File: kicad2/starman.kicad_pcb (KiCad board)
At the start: 4 copper layers, 195 x 150 mm, 202 parts, among them J1 Conn_01x12, J10 Barrel_Jack_MountingPin, J2 Conn_01x10, J3 Conn_01x12, J4 Conn_01x06, J5 Conn_02x03_Counter_Clockwise, J6 Conn_01x12, J7 Conn_01x10, J8 Conn_01x12, J9 Conn_01x08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

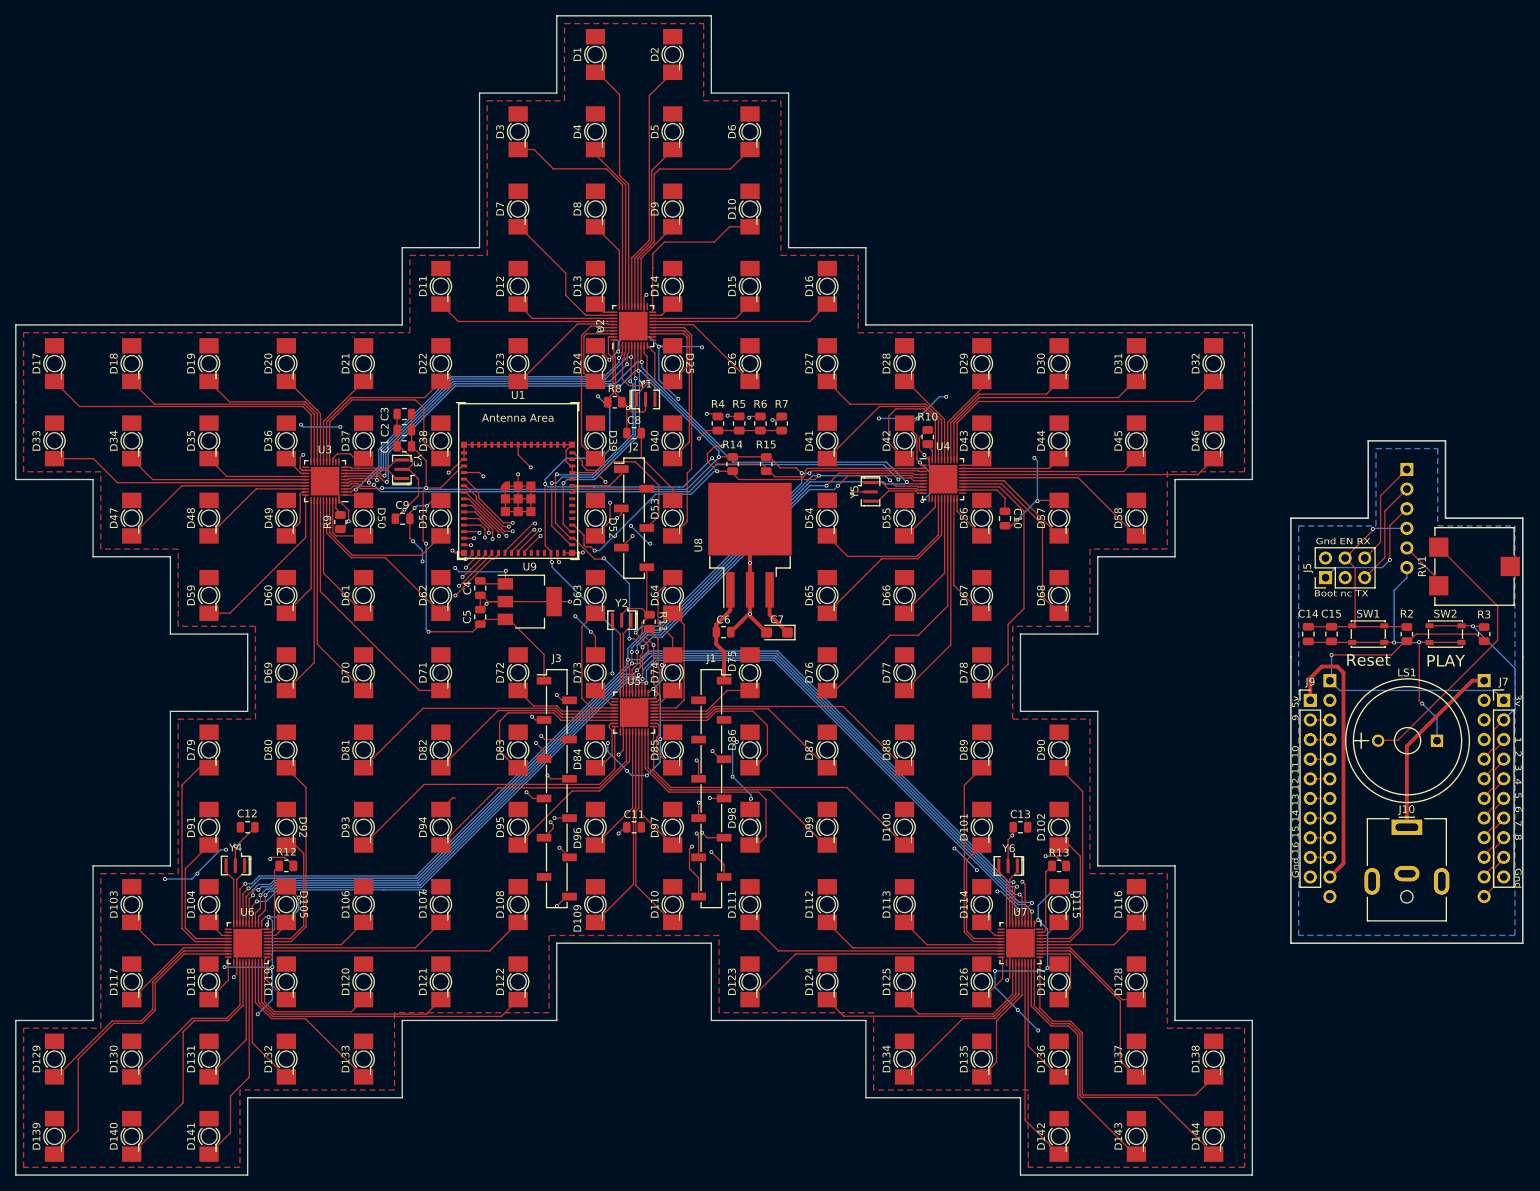
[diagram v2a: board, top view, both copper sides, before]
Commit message: Added dimensions and a label
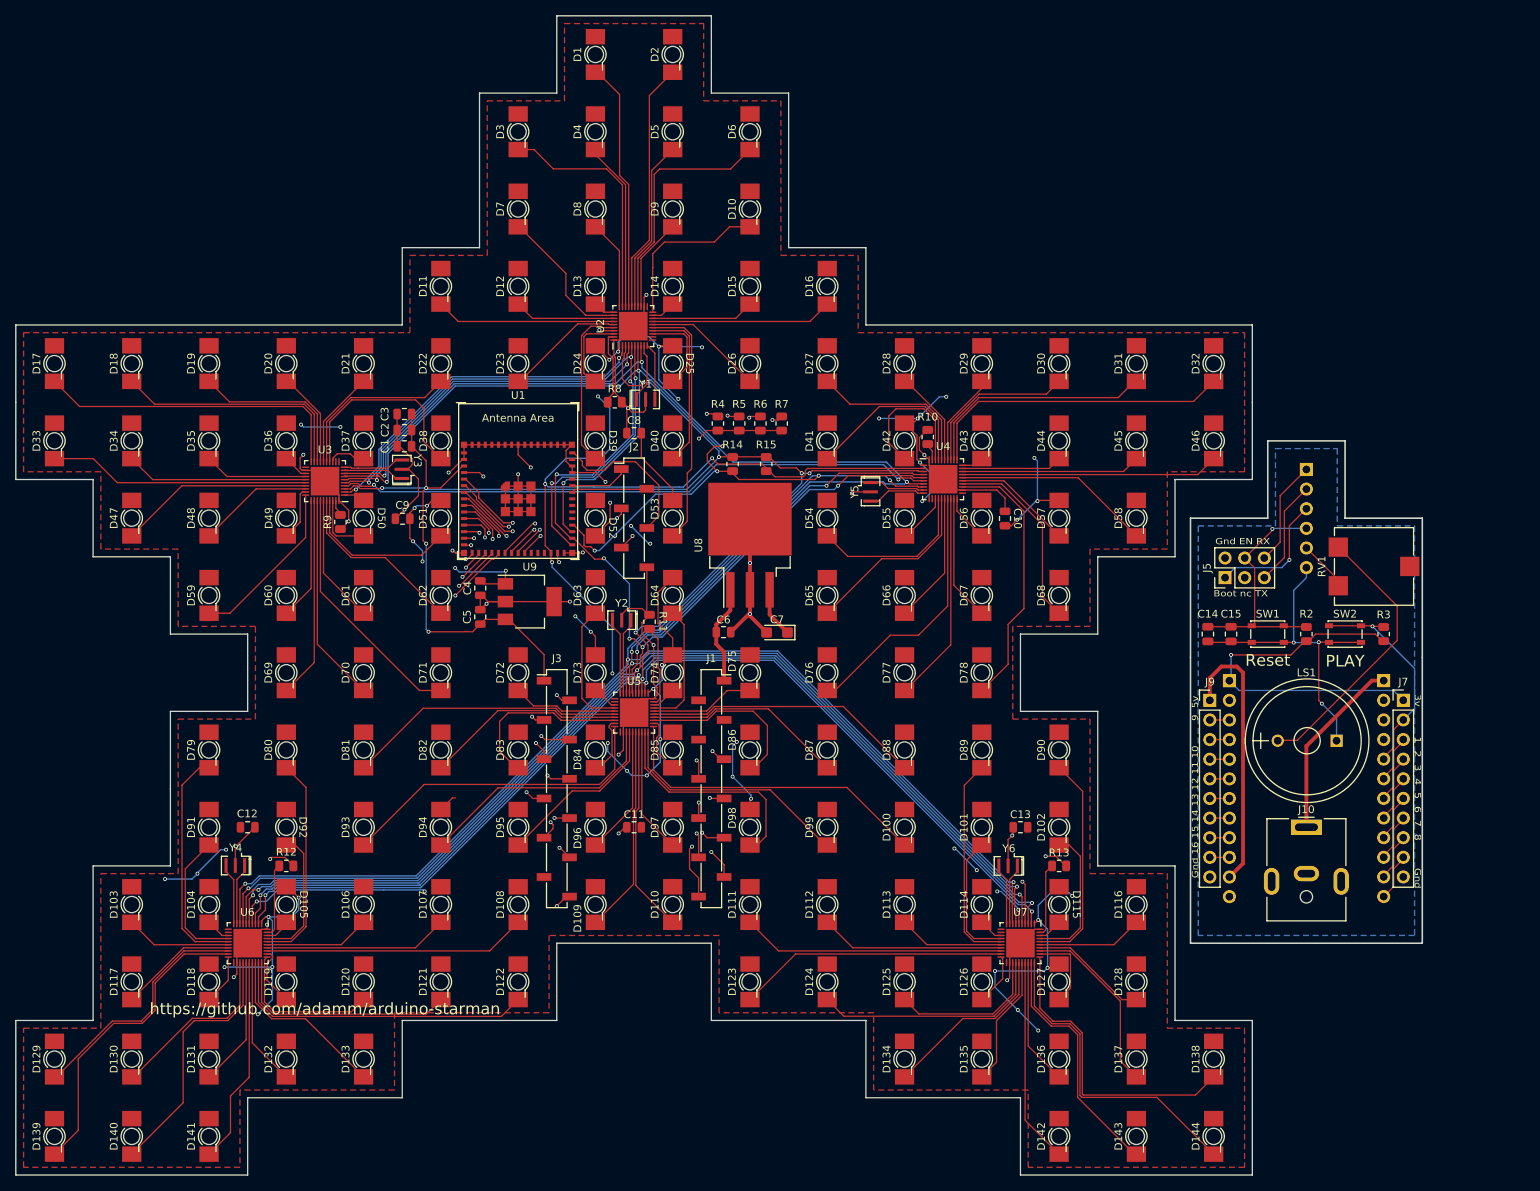
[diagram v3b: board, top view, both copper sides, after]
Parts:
- moved C14 13.0 mm to (184.2, 110.0)
- moved C15 13.0 mm to (187.2, 110.0)
- moved J10 13.0 mm to (197.0, 135.0)
- moved J4 13.0 mm to (197.0, 88.7)
- moved J5 13.0 mm to (186.5, 102.7)
- moved J6 13.0 mm to (207.0, 116.0)
- moved J7 13.0 mm to (209.5, 118.6)
- moved J8 13.0 mm to (187.0, 116.0)
- moved J9 13.0 mm to (184.5, 118.6)
- moved LS1 13.0 mm to (200.9, 123.8)
- moved R2 13.0 mm to (197.0, 110.0)
- moved R3 13.0 mm to (207.0, 110.0)
- moved RV1 13.0 mm to (205.8, 101.2)
- moved SW1 13.0 mm to (192.0, 110.0)
- moved SW2 13.0 mm to (202.0, 110.0)
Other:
- board size 195 x 150 mm -> 182 x 150 mm
- rule pad_to_mask_clearance: 0.05 -> 0
- board text added: "https://github.com/adamm/arduino-starman"
